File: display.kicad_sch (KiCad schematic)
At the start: 1 part, among them J3 AXF5D3012

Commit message: added buck
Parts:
- added C6, C9: C_Small, symbol Device:C_Small
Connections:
- net +1V8: now also C6.1, C9.1
- net GND: now also C6.2, C9.2
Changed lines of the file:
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@@
 (kicad_sch (version 20230121) (generator eeschema)
   (paper "A4")
+  (junction (at 33.02 69.85) (diameter 0) (color 0 0 0 0)
+  )
   (junction (at 139.7 127) (diameter 0) (color 0 0 0 0)
   )
   (junction (at 137.16 63.5) (diameter 0) (color 0 0 0 0)
   )
+  (junction (at 45.72 69.85) (diameter 0) (color 0 0 0 0)
+  )
   (junction (at 143.51 63.5) (diameter 0) (color 0 0 0 0)
   )
@@
     (stroke (width 0) (type default))
   )
-  (wire (pts (xy 52.07 52.07) (xy 52.07 54.61))
-    (stroke (width 0) (type default))
-  )
   (wire (pts (xy 168.91 95.25) (xy 171.45 95.25))
     (stroke (width 0) (type default))
@@
     (stroke (width 0) (type default))
   )
+  (wire (pts (xy 33.02 67.31) (xy 33.02 69.85))
+    (stroke (width 0) (type default))
+  )
   (wire (pts (xy 137.16 63.5) (xy 139.7 63.5))
     (stroke (width 0) (type default))
@@
     (stroke (width 0) (type default))
   )
-  (wire (pts (xy 54.61 54.61) (xy 52.07 54.61))
-    (stroke (width 0) (type default))
-  )
   (wire (pts (xy 137.16 63.5) (xy 137.16 66.04))
     (stroke (width 0) (type default))
@@
     (stroke (width 0) (type default))
   )
+  (wire (pts (xy 45.72 69.85) (xy 50.8 69.85))
+    (stroke (width 0) (type default))
+  )
   (wire (pts (xy 110.49 90.17) (xy 113.03 90.17))
     (stroke (width 0) (type default))
@@
     (stroke (width 0) (type default))
   )
+  (wire (pts (xy 33.02 69.85) (xy 45.72 69.85))
+    (stroke (width 0) (type default))
+  )
   (wire (pts (xy 110.49 97.79) (xy 113.03 97.79))
     (stroke (width 0) (type default))
   )
+  (wire (pts (xy 33.02 74.93) (xy 33.02 77.47))
+    (stroke (width 0) (type default))
+  )
   (wire (pts (xy 139.7 124.46) (xy 139.7 127))
     (stroke (width 0) (type default))
@@
   )
   (wire (pts (xy 52.07 41.91) (xy 52.07 44.45))
+    (stroke (width 0) (type default))
+  )
+  (wire (pts (xy 45.72 74.93) (xy 45.72 77.47))
     (stroke (width 0) (type default))
   )
@@
     )
   )
-  (global_label "VIO18" (shape input) (at 54.61 54.61 0) (fields_autoplaced)
-    (effects (font (size 1.27 1.27)) (justify left))
-    (property "Intersheetrefs" "${INTERSHEET_REFS}" (at 62.9587 54.61 0)
-      (effects (font (size 1.27 1.27)) (justify left) hide)
-    )
-  )
   (global_label "NFC_ANT2" (shape input) (at 110.49 105.41 180) (fields_autoplaced)
     (effects (font (size 1.27 1.27)) (justify right))
@@
     )
   )
+  (global_label "VIO18" (shape input) (at 50.8 69.85 0) (fields_autoplaced)
+    (effects (font (size 1.27 1.27)) (justify left))
+    (property "Intersheetrefs" "${INTERSHEET_REFS}" (at 59.1487 69.85 0)
+      (effects (font (size 1.27 1.27)) (justify left) hide)
+    )
+  )
   (global_label "VPH_PWR" (shape input) (at 137.16 60.96 90) (fields_autoplaced)
     (effects (font (size 1.27 1.27)) (justify left))
@@
     )
   )
+  (symbol (lib_id "power:+1V8") (at 33.02 67.31 0) (unit 1)
+    (in_bom yes) (on_board yes) (dnp no) (fields_autoplaced)
+    (property "Reference" "#PWR028" (at 33.02 71.12 0)
+      (effects (font (size 1.27 1.27)) hide)
+    )
+    (property "Value" "+1V8" (at 33.02 63.5 0)
+      (effects (font (size 1.27 1.27)))
+    )
+    (property "Footprint" "" (at 33.02 67.31 0)
+      (effects (font (size 1.27 1.27)) hide)
+    )
+    (property "Datasheet" "" (at 33.02 67.31 0)
+      (effects (font (size 1.27 1.27)) hide)
+    )
+    (pin "1")
+    (instances
+      (project "armband"
+        (path "/017c50c6-333c-4d31-ad5a-278994a09b14"
+          (reference "#PWR028") (unit 1)
+        )
+        (path "/017c50c6-333c-4d31-ad5a-278994a09b14/ae5dc462-dca9-40e4-ba02-6b87a86a4904"
+          (reference "#PWR028") (unit 1)
+        )
+        (path "/017c50c6-333c-4d31-ad5a-278994a09b14/ea4ffdec-697e-4619-8bda-0f4c7cf70f55"
+          (reference "#PWR028") (unit 1)
+        )
+      )
+    )
+  )
   (symbol (lib_id "power:+3V3") (at 52.07 41.91 0) (unit 1)
     (in_bom yes) (on_board yes) (dnp no) (fields_autoplaced)
@@
         )
         (path "/017c50c6-333c-4d31-ad5a-278994a09b14/ea4ffdec-697e-4619-8bda-0f4c7cf70f55"
-          (reference "#PWR010") (unit 1)
+          (reference "#PWR013") (unit 1)
+        )
+      )
+    )
+  )
+  (symbol (lib_id "Device:C_Small") (at 45.72 72.39 0) (mirror y) (unit 1)
+    (in_bom yes) (on_board yes) (dnp no) (fields_autoplaced)
+    (property "Reference" "C9" (at 48.26 71.7613 0)
+      (effects (font (size 1.27 1.27)) (justify right))
+    )
+    (property "Value" "C_Small" (at 48.26 74.3013 0)
+      (effects (font (size 1.27 1.27)) (justify right))
+    )
+    (property "Footprint" "" (at 45.72 72.39 0)
+      (effects (font (size 1.27 1.27)) hide)
+    )
+    (property "Datasheet" "~" (at 45.72 72.39 0)
+      (effects (font (size 1.27 1.27)) hide)
+    )
+    (pin "1")
+    (pin "2")
+    (instances
+      (project "armband"
+        (path "/017c50c6-333c-4d31-ad5a-278994a09b14"
+          (reference "C9") (unit 1)
+        )
+        (path "/017c50c6-333c-4d31-ad5a-278994a09b14/ae5dc462-dca9-40e4-ba02-6b87a86a4904"
+          (reference "C9") (unit 1)
+        )
+        (path "/017c50c6-333c-4d31-ad5a-278994a09b14/ea4ffdec-697e-4619-8bda-0f4c7cf70f55"
+          (reference "C9") (unit 1)
         )
       )
@@
         )
         (path "/017c50c6-333c-4d31-ad5a-278994a09b14/ea4ffdec-697e-4619-8bda-0f4c7cf70f55"
-          (reference "#PWR012") (unit 1)
-        )
-      )
-    )
-  )
-  (symbol (lib_id "power:+1V8") (at 52.07 52.07 0) (unit 1)
-    (in_bom yes) (on_board yes) (dnp no) (fields_autoplaced)
-    (property "Reference" "#PWR087" (at 52.07 55.88 0)
-      (effects (font (size 1.27 1.27)) hide)
-    )
-    (property "Value" "+1V8" (at 52.07 48.26 0)
-      (effects (font (size 1.27 1.27)))
-    )
-    (property "Footprint" "" (at 52.07 52.07 0)
-      (effects (font (size 1.27 1.27)) hide)
-    )
-    (property "Datasheet" "" (at 52.07 52.07 0)
-      (effects (font (size 1.27 1.27)) hide)
-    )
-    (pin "1")
-    (instances
-      (project "armband"
-        (path "/017c50c6-333c-4d31-ad5a-278994a09b14"
-          (reference "#PWR087") (unit 1)
-        )
-        (path "/017c50c6-333c-4d31-ad5a-278994a09b14/ea4ffdec-697e-4619-8bda-0f4c7cf70f55"
-          (reference "#PWR011") (unit 1)
+          (reference "#PWR015") (unit 1)
+        )
+      )
+    )
+  )
+  (symbol (lib_id "power:GND") (at 33.02 77.47 0) (unit 1)
+    (in_bom yes) (on_board yes) (dnp no) (fields_autoplaced)
+    (property "Reference" "#PWR029" (at 33.02 83.82 0)
+      (effects (font (size 1.27 1.27)) hide)
+    )
+    (property "Value" "GND" (at 33.02 82.55 0)
+      (effects (font (size 1.27 1.27)))
+    )
+    (property "Footprint" "" (at 33.02 77.47 0)
+      (effects (font (size 1.27 1.27)) hide)
+    )
+    (property "Datasheet" "" (at 33.02 77.47 0)
+      (effects (font (size 1.27 1.27)) hide)
+    )
+    (pin "1")
+    (instances
+      (project "armband"
+        (path "/017c50c6-333c-4d31-ad5a-278994a09b14"
+          (reference "#PWR029") (unit 1)
+        )
+        (path "/017c50c6-333c-4d31-ad5a-278994a09b14/ae5dc462-dca9-40e4-ba02-6b87a86a4904"
+          (reference "#PWR029") (unit 1)
+        )
+        (path "/017c50c6-333c-4d31-ad5a-278994a09b14/ea4ffdec-697e-4619-8bda-0f4c7cf70f55"
+          (reference "#PWR029") (unit 1)
         )
       )
@@
         )
         (path "/017c50c6-333c-4d31-ad5a-278994a09b14/ea4ffdec-697e-4619-8bda-0f4c7cf70f55"
-          (reference "#PWR013") (unit 1)
+          (reference "#PWR016") (unit 1)
         )
       )
@@
         )
       )
+    )
+  )
+  (symbol (lib_id "power:GND") (at 45.72 77.47 0) (unit 1)
+    (in_bom yes) (on_board yes) (dnp no) (fields_autoplaced)
+    (property "Reference" "#PWR032" (at 45.72 83.82 0)
+      (effects (font (size 1.27 1.27)) hide)
+    )
+    (property "Value" "GND" (at 45.72 82.55 0)
+      (effects (font (size 1.27 1.27)))
+    )
+    (property "Footprint" "" (at 45.72 77.47 0)
+      (effects (font (size 1.27 1.27)) hide)
+    )
+    (property "Datasheet" "" (at 45.72 77.47 0)
+      (effects (font (size 1.27 1.27)) hide)
+    )
+    (pin "1")
+    (instances
+      (project "armband"
+        (path "/017c50c6-333c-4d31-ad5a-278994a09b14"
+          (reference "#PWR032") (unit 1)
+        )
+        (path "/017c50c6-333c-4d31-ad5a-278994a09b14/ae5dc462-dca9-40e4-ba02-6b87a86a4904"
+          (reference "#PWR032") (unit 1)
+        )
+        (path "/017c50c6-333c-4d31-ad5a-278994a09b14/ea4ffdec-697e-4619-8bda-0f4c7cf70f55"
+          (reference "#PWR032") (unit 1)
+        )
+      )
+    )
+  )
+  (symbol (lib_id "Device:C_Small") (at 33.02 72.39 0) (mirror y) (unit 1)
+    (in_bom yes) (on_board yes) (dnp no) (fields_autoplaced)
+    (property "Reference" "C6" (at 35.56 71.7613 0)
+      (effects (font (size 1.27 1.27)) (justify right))
+    )
+    (property "Value" "C_Small" (at 35.56 74.3013 0)
+      (effects (font (size 1.27 1.27)) (justify right))
+    )
+    (property "Footprint" "" (at 33.02 72.39 0)
+      (effects (font (size 1.27 1.27)) hide)
+    )
+    (property "Datasheet" "~" (at 33.02 72.39 0)
+      (effects (font (size 1.27 1.27)) hide)
+    )
+    (pin "1")
+    (pin "2")
+    (instances
+      (project "armband"
+        (path "/017c50c6-333c-4d31-ad5a-278994a09b14"
+          (reference "C6") (unit 1)
+        )
+        (path "/017c50c6-333c-4d31-ad5a-278994a09b14/ae5dc462-dca9-40e4-ba02-6b87a86a4904"
+          (reference "C6") (unit 1)
+        )
+        (path "/017c50c6-333c-4d31-ad5a-278994a09b14/ea4ffdec-697e-4619-8bda-0f4c7cf70f55"
+          (reference "C6") (unit 1)
+        )
+      )

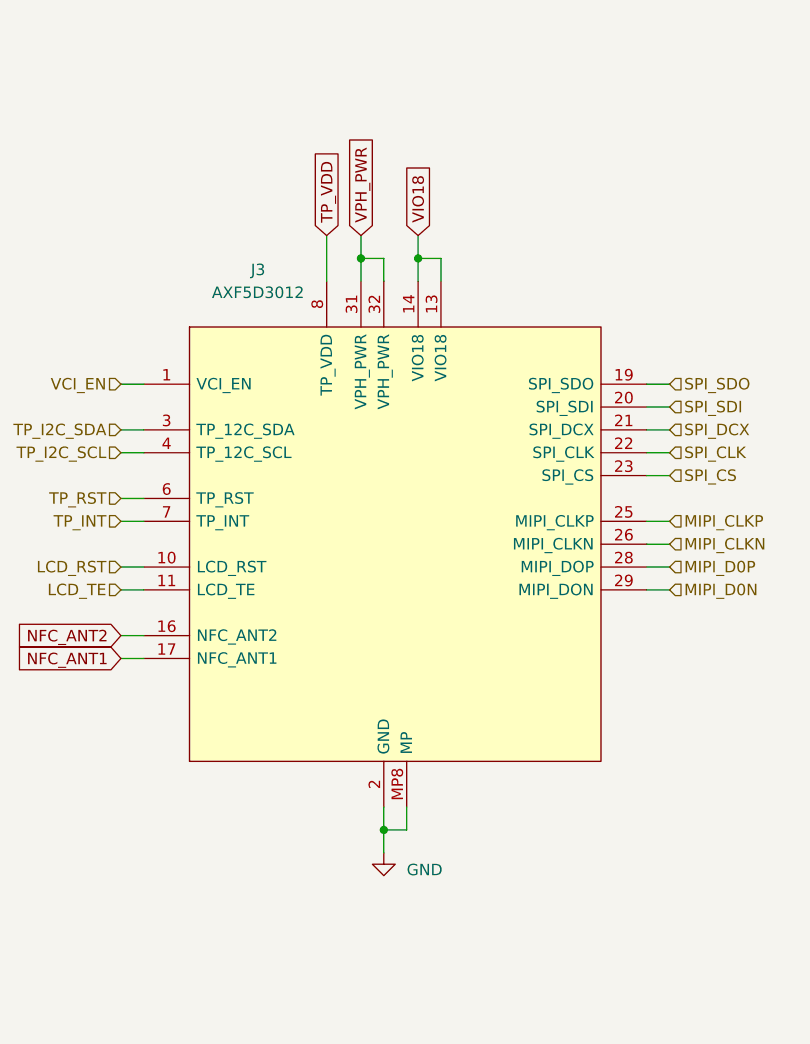
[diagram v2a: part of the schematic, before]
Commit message: fixed display connector
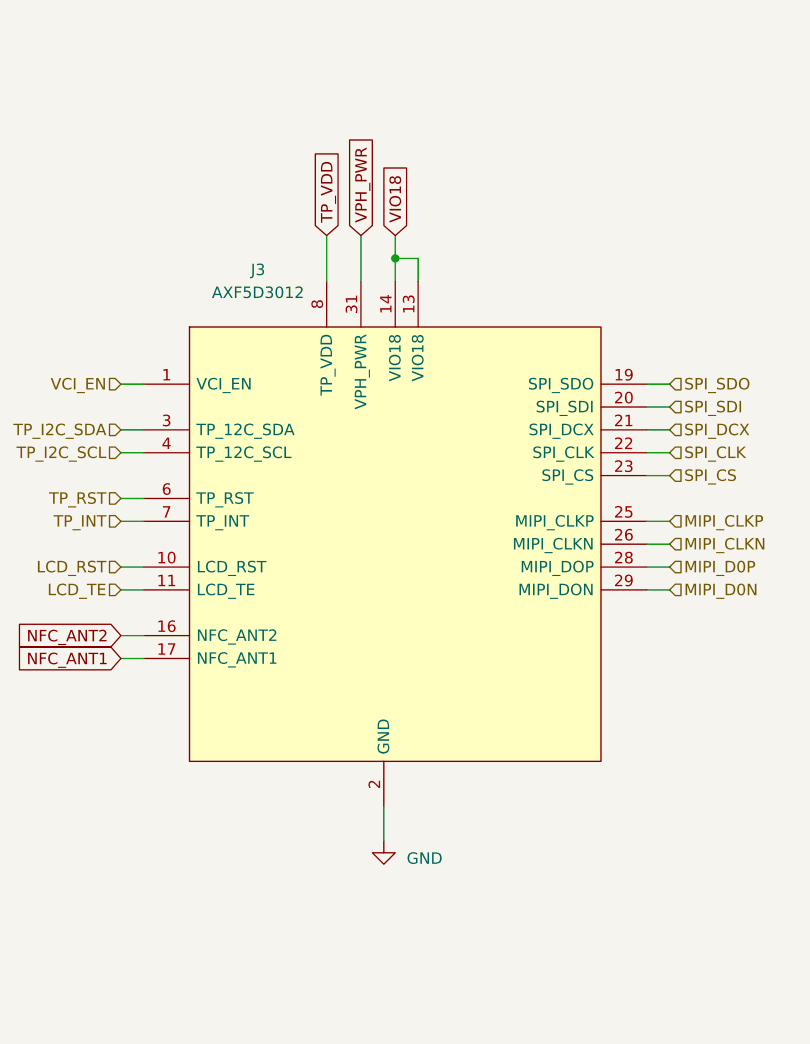
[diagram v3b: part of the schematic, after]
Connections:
- net +3V3: no longer J3.32 (VPH_PWR)
- net GND: no longer J3.MP5 (MP), J3.MP6 (MP), J3.MP7 (MP), J3.MP8 (MP)
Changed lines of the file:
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@@
   (junction (at 33.02 69.85) (diameter 0) (color 0 0 0 0)
   )
-  (junction (at 139.7 127) (diameter 0) (color 0 0 0 0)
-  )
-  (junction (at 137.16 63.5) (diameter 0) (color 0 0 0 0)
-  )
   (junction (at 45.72 69.85) (diameter 0) (color 0 0 0 0)
   )
-  (junction (at 143.51 63.5) (diameter 0) (color 0 0 0 0)
+  (junction (at 140.97 63.5) (diameter 0) (color 0 0 0 0)
   )
   (wire (pts (xy 54.61 44.45) (xy 52.07 44.45))
@@
     (stroke (width 0) (type default))
   )
-  (wire (pts (xy 137.16 63.5) (xy 139.7 63.5))
-    (stroke (width 0) (type default))
-  )
   (wire (pts (xy 110.49 105.41) (xy 113.03 105.41))
     (stroke (width 0) (type default))
   )
-  (wire (pts (xy 146.05 63.5) (xy 146.05 66.04))
+  (wire (pts (xy 143.51 63.5) (xy 143.51 66.04))
     (stroke (width 0) (type default))
   )
@@
     (stroke (width 0) (type default))
   )
-  (wire (pts (xy 137.16 63.5) (xy 137.16 66.04))
+  (wire (pts (xy 137.16 60.96) (xy 137.16 66.04))
     (stroke (width 0) (type default))
   )
@@
     (stroke (width 0) (type default))
   )
-  (wire (pts (xy 142.24 127) (xy 142.24 124.46))
-    (stroke (width 0) (type default))
-  )
   (wire (pts (xy 168.91 85.09) (xy 171.45 85.09))
     (stroke (width 0) (type default))
@@
     (stroke (width 0) (type default))
   )
-  (wire (pts (xy 139.7 66.04) (xy 139.7 63.5))
-    (stroke (width 0) (type default))
-  )
   (wire (pts (xy 110.49 100.33) (xy 113.03 100.33))
     (stroke (width 0) (type default))
@@
     (stroke (width 0) (type default))
   )
-  (wire (pts (xy 139.7 124.46) (xy 139.7 127))
-    (stroke (width 0) (type default))
-  )
   (wire (pts (xy 110.49 107.95) (xy 113.03 107.95))
     (stroke (width 0) (type default))
@@
     (stroke (width 0) (type default))
   )
-  (wire (pts (xy 139.7 127) (xy 142.24 127))
-    (stroke (width 0) (type default))
-  )
-  (wire (pts (xy 137.16 60.96) (xy 137.16 63.5))
-    (stroke (width 0) (type default))
-  )
-  (wire (pts (xy 143.51 60.96) (xy 143.51 63.5))
+  (wire (pts (xy 140.97 60.96) (xy 140.97 63.5))
     (stroke (width 0) (type default))
   )
@@
     (stroke (width 0) (type default))
   )
-  (wire (pts (xy 143.51 66.04) (xy 143.51 63.5))
-    (stroke (width 0) (type default))
-  )
-  (wire (pts (xy 143.51 63.5) (xy 146.05 63.5))
-    (stroke (width 0) (type default))
-  )
-  (wire (pts (xy 139.7 127) (xy 139.7 129.54))
+  (wire (pts (xy 140.97 66.04) (xy 140.97 63.5))
+    (stroke (width 0) (type default))
+  )
+  (wire (pts (xy 140.97 63.5) (xy 143.51 63.5))
+    (stroke (width 0) (type default))
+  )
+  (wire (pts (xy 139.7 124.46) (xy 139.7 128.27))
     (stroke (width 0) (type default))
   )
@@
     )
   )
-  (global_label "VIO18" (shape input) (at 143.51 60.96 90) (fields_autoplaced)
-    (effects (font (size 1.27 1.27)) (justify left))
-    (property "Intersheetrefs" "${INTERSHEET_REFS}" (at 143.51 52.6113 90)
+  (global_label "VIO18" (shape input) (at 140.97 60.96 90) (fields_autoplaced)
+    (effects (font (size 1.27 1.27)) (justify left))
+    (property "Intersheetrefs" "${INTERSHEET_REFS}" (at 140.97 52.6113 90)
       (effects (font (size 1.27 1.27)) (justify left) hide)
     )
@@
     )
   )
-  (symbol (lib_id "power:GND") (at 139.7 129.54 0) (unit 1)
-    (in_bom yes) (on_board yes) (dnp no) (fields_autoplaced)
-    (property "Reference" "#PWR093" (at 139.7 135.89 0)
-      (effects (font (size 1.27 1.27)) hide)
-    )
-    (property "Value" "GND" (at 142.24 131.445 0)
+  (symbol (lib_id "power:GND") (at 139.7 128.27 0) (unit 1)
+    (in_bom yes) (on_board yes) (dnp no) (fields_autoplaced)
+    (property "Reference" "#PWR093" (at 139.7 134.62 0)
+      (effects (font (size 1.27 1.27)) hide)
+    )
+    (property "Value" "GND" (at 142.24 130.175 0)
       (effects (font (size 1.27 1.27)) (justify left))
     )
-    (property "Footprint" "" (at 139.7 129.54 0)
-      (effects (font (size 1.27 1.27)) hide)
-    )
-    (property "Datasheet" "" (at 139.7 129.54 0)
+    (property "Footprint" "" (at 139.7 128.27 0)
+      (effects (font (size 1.27 1.27)) hide)
+    )
+    (property "Datasheet" "" (at 139.7 128.27 0)
       (effects (font (size 1.27 1.27)) hide)
     )
@@
     (pin "3")
     (pin "31")
-    (pin "32")
     (pin "4")
     (pin "6")
     (pin "7")
     (pin "8")
-    (pin "MP8")
     (pin "12")
     (pin "15")
@@
     (pin "5")
     (pin "9")
-    (pin "MP5")
-    (pin "MP6")
-    (pin "MP7")
-    (instances
-      (project "armband"
+    (instances
+      (project "armband"

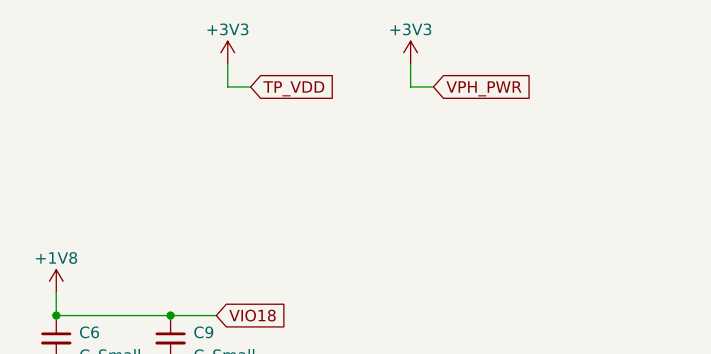
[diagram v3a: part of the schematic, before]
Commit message: added decoupling capacitors to sensors
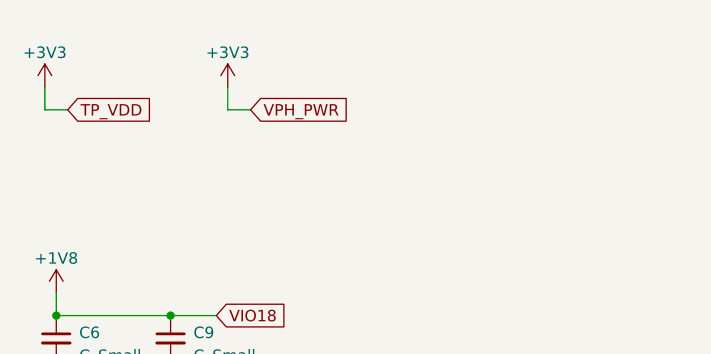
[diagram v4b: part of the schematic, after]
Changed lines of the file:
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@@
   (junction (at 140.97 63.5) (diameter 0) (color 0 0 0 0)
   )
-  (wire (pts (xy 54.61 44.45) (xy 52.07 44.45))
+  (wire (pts (xy 34.29 46.99) (xy 31.75 46.99))
     (stroke (width 0) (type default))
   )
@@
     (stroke (width 0) (type default))
   )
-  (wire (pts (xy 74.93 44.45) (xy 72.39 44.45))
+  (wire (pts (xy 54.61 46.99) (xy 52.07 46.99))
     (stroke (width 0) (type default))
   )
@@
     (stroke (width 0) (type default))
   )
-  (wire (pts (xy 72.39 41.91) (xy 72.39 44.45))
+  (wire (pts (xy 52.07 44.45) (xy 52.07 46.99))
     (stroke (width 0) (type default))
   )
@@
     (stroke (width 0) (type default))
   )
-  (wire (pts (xy 52.07 41.91) (xy 52.07 44.45))
+  (wire (pts (xy 31.75 44.45) (xy 31.75 46.99))
     (stroke (width 0) (type default))
   )
@@
     )
   )
-  (global_label "TP_VDD" (shape input) (at 54.61 44.45 0) (fields_autoplaced)
-    (effects (font (size 1.27 1.27)) (justify left))
-    (property "Intersheetrefs" "${INTERSHEET_REFS}" (at 64.3496 44.45 0)
-      (effects (font (size 1.27 1.27)) (justify left) hide)
-    )
-  )
-  (global_label "VPH_PWR" (shape input) (at 74.93 44.45 0) (fields_autoplaced)
-    (effects (font (size 1.27 1.27)) (justify left))
-    (property "Intersheetrefs" "${INTERSHEET_REFS}" (at 86.4839 44.45 0)
+  (global_label "TP_VDD" (shape input) (at 34.29 46.99 0) (fields_autoplaced)
+    (effects (font (size 1.27 1.27)) (justify left))
+    (property "Intersheetrefs" "${INTERSHEET_REFS}" (at 44.0296 46.99 0)
+      (effects (font (size 1.27 1.27)) (justify left) hide)
+    )
+  )
+  (global_label "VPH_PWR" (shape input) (at 54.61 46.99 0) (fields_autoplaced)
+    (effects (font (size 1.27 1.27)) (justify left))
+    (property "Intersheetrefs" "${INTERSHEET_REFS}" (at 66.1639 46.99 0)
       (effects (font (size 1.27 1.27)) (justify left) hide)
     )
@@
     )
   )
-  (symbol (lib_id "power:+3V3") (at 52.07 41.91 0) (unit 1)
+  (symbol (lib_id "power:+3V3") (at 31.75 44.45 0) (unit 1)
     (in_bom yes) (on_board yes) (dnp no) (fields_autoplaced)
-    (property "Reference" "#PWR086" (at 52.07 45.72 0)
-      (effects (font (size 1.27 1.27)) hide)
-    )
-    (property "Value" "+3V3" (at 52.07 38.1 0)
+    (property "Reference" "#PWR086" (at 31.75 48.26 0)
+      (effects (font (size 1.27 1.27)) hide)
+    )
+    (property "Value" "+3V3" (at 31.75 40.64 0)
       (effects (font (size 1.27 1.27)))
     )
-    (property "Footprint" "" (at 52.07 41.91 0)
-      (effects (font (size 1.27 1.27)) hide)
-    )
-    (property "Datasheet" "" (at 52.07 41.91 0)
+    (property "Footprint" "" (at 31.75 44.45 0)
+      (effects (font (size 1.27 1.27)) hide)
+    )
+    (property "Datasheet" "" (at 31.75 44.45 0)
       (effects (font (size 1.27 1.27)) hide)
     )
@@
     )
   )
-  (symbol (lib_id "power:+3V3") (at 72.39 41.91 0) (unit 1)
+  (symbol (lib_id "power:+3V3") (at 52.07 44.45 0) (unit 1)
     (in_bom yes) (on_board yes) (dnp no) (fields_autoplaced)
-    (property "Reference" "#PWR095" (at 72.39 45.72 0)
-      (effects (font (size 1.27 1.27)) hide)
-    )
-    (property "Value" "+3V3" (at 72.39 38.1 0)
+    (property "Reference" "#PWR095" (at 52.07 48.26 0)
+      (effects (font (size 1.27 1.27)) hide)
+    )
+    (property "Value" "+3V3" (at 52.07 40.64 0)
       (effects (font (size 1.27 1.27)))
     )
-    (property "Footprint" "" (at 72.39 41.91 0)
-      (effects (font (size 1.27 1.27)) hide)
-    )
-    (property "Datasheet" "" (at 72.39 41.91 0)
-      (effects (font (size 1.27 1.27)) hide)
-    )
+    (property "Footprint" "" (at 52.07 44.45 0)
+      (effects (font (size 1.27 1.27)) hide)
+    )
+    (property "Datasheet" "" (at 52.07 44.45 0)
+      (effects (font (size 1.27 1.27)) hide)
+    )
